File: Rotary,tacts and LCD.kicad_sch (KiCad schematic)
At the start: 53 parts, among them Q1 MMBT3904, SW1 EC11E18244AU, U14 RT9193-18GB, U4 AP3032KTR-G1, U7 IS31FL3733B-QFLS4-TR

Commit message: Updated the net labels for 3v3 and sys rail
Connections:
- net +3V3 is gone; now on net ESP_3V3: C21.1, C22.1, C23.1, C24.1, C25.1, C26.1, C27.1, R10.1, R9.1, U7.20 (PVCC_1), U7.29 (PVCC_2), U7.37 (AVCC), U7.38 (DVCC), U7.39 (VIO)
- net Core_5V renamed SYS

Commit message: Did the layout plan
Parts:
- removed L1: 10uH 3×3×1.5 0.72A, symbol Device:L
- added L1: SWPA3015S100MT, SWPA3015S100MT:IND-SMD_L3.0-W3.0_SWPA3010S, symbol SWPA3015S100MT:SWPA3015S100MT
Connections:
- net SYS: now also L1.1
- net at D31.2, U4.1 (SW): now also L1.2
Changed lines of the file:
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@@
 	(wire
 		(pts
+			(xy 87.63 204.47) (xy 101.6 204.47)
+		)
+		(stroke
+			(width 0)
+			(type default)
+		)
+	)
+	(wire
+		(pts
 			(xy 403.86 102.87) (xy 422.91 102.87)
 		)
@@
 	(wire
 		(pts
+			(xy 64.77 204.47) (xy 77.47 204.47)
+		)
+		(stroke
+			(width 0)
+			(type default)
+		)
+	)
+	(wire
+		(pts
 			(xy 346.71 182.88) (xy 346.71 186.69)
 		)
@@
 	(wire
 		(pts
-			(xy 78.74 204.47) (xy 64.77 204.47)
-		)
-		(stroke
-			(width 0)
-			(type default)
-		)
-	)
-	(wire
-		(pts
 			(xy 208.28 86.36) (xy 212.09 86.36)
 		)
@@
 	(wire
 		(pts
-			(xy 86.36 204.47) (xy 101.6 204.47)
-		)
-		(stroke
-			(width 0)
-			(type default)
-		)
-	)
-	(wire
-		(pts
 			(xy 374.65 82.55) (xy 367.03 82.55)
 		)
@@
 	)
 	(symbol
-		(lib_id "Device:L")
-		(at 82.55 204.47 90)
-		(unit 1)
-		(body_style 1)
-		(exclude_from_sim no)
-		(in_bom yes)
-		(on_board yes)
-		(in_pos_files yes)
-		(dnp no)
-		(fields_autoplaced yes)
-		(property "Reference" "L1"
-			(at 82.55 199.39 90)
-			(show_name no)
-			(do_not_autoplace no)
-			(effects
-				(font
-					(size 1.27 1.27)
-				)
-			)
-		)
-		(property "Value" "10uH 3×3×1.5 0.72A"
-			(at 82.55 201.93 90)
-			(show_name no)
-			(do_not_autoplace no)
-			(effects
-				(font
-					(size 1.27 1.27)
-				)
-			)
-		)
-		(property "Footprint" ""
-			(at 82.55 204.47 0)
-			(hide yes)
-			(show_name no)
-			(do_not_autoplace no)
-			(effects
-				(font
-					(size 1.27 1.27)
-				)
-			)
-		)
-		(property "Datasheet" ""
-			(at 82.55 204.47 0)
-			(hide yes)
-			(show_name no)
-			(do_not_autoplace no)
-			(effects
-				(font
-					(size 1.27 1.27)
-				)
-			)
-		)
-		(property "Description" "Inductor"
-			(at 82.55 204.47 0)
-			(hide yes)
-			(show_name no)
-			(do_not_autoplace no)
-			(effects
-				(font
-					(size 1.27 1.27)
-				)
-			)
-		)
-		(property "Availability" ""
-			(at 82.55 204.47 90)
-			(hide yes)
-			(show_name no)
-			(do_not_autoplace no)
-			(effects
-				(font
-					(size 1.27 1.27)
-				)
-			)
-		)
-		(property "Check_prices" ""
-			(at 82.55 204.47 90)
-			(hide yes)
-			(show_name no)
-			(do_not_autoplace no)
-			(effects
-				(font
-					(size 1.27 1.27)
-				)
-			)
-		)
-		(property "Height" ""
-			(at 82.55 204.47 90)
-			(hide yes)
-			(show_name no)
-			(do_not_autoplace no)
-			(effects
-				(font
-					(size 1.27 1.27)
-				)
-			)
-		)
-		(property "MF" ""
-			(at 82.55 204.47 90)
-			(hide yes)
-			(show_name no)
-			(do_not_autoplace no)
-			(effects
-				(font
-					(size 1.27 1.27)
-				)
-			)
-		)
-		(property "MP" ""
-			(at 82.55 204.47 90)
-			(hide yes)
-			(show_name no)
-			(do_not_autoplace no)
-			(effects
-				(font
-					(size 1.27 1.27)
-				)
-			)
-		)
-		(property "Manufacturer_Name" ""
-			(at 82.55 204.47 90)
-			(hide yes)
-			(show_name no)
-			(do_not_autoplace no)
-			(effects
-				(font
-					(size 1.27 1.27)
-				)
-			)
-		)
-		(property "Manufacturer_Part_Number" ""
-			(at 82.55 204.47 90)
-			(hide yes)
-			(show_name no)
-			(do_not_autoplace no)
-			(effects
-				(font
-					(size 1.27 1.27)
-				)
-			)
-		)
-		(property "Mouser Part Number" ""
-			(at 82.55 204.47 90)
-			(hide yes)
-			(show_name no)
-			(do_not_autoplace no)
-			(effects
-				(font
-					(size 1.27 1.27)
-				)
-			)
-		)
-		(property "Mouser Price/Stock" ""
-			(at 82.55 204.47 90)
-			(hide yes)
-			(show_name no)
-			(do_not_autoplace no)
-			(effects
-				(font
-					(size 1.27 1.27)
-				)
-			)
-		)
-		(property "Package" ""
-			(at 82.55 204.47 90)
-			(hide yes)
-			(show_name no)
-			(do_not_autoplace no)
-			(effects
-				(font
-					(size 1.27 1.27)
-				)
-			)
-		)
-		(property "STANDARD" ""
-			(at 82.55 204.47 90)
-			(hide yes)
-			(show_name no)
-			(do_not_autoplace no)
-			(effects
-				(font
-					(size 1.27 1.27)
-				)
-			)
-		)
-		(property "SnapEDA_Link" ""
-			(at 82.55 204.47 90)
-			(hide yes)
-			(show_name no)
-			(do_not_autoplace no)
-			(effects
-				(font
-					(size 1.27 1.27)
-				)
-			)
-		)
-		(pin "2"
-		)
-		(pin "1"
-		)
-		(instances
-			(project "Galatea Keyboard PCB"
-				(path "/04167948-25c2-4ca8-b9d8-855756010414/f6cda99c-23a6-4328-98ed-312da4a40ab9"
-					(reference "L1")
-					(unit 1)
-				)
-			)
-		)
-	)
-	(symbol
 		(lib_id "Device:C_Small")
 		(at 43.18 349.25 0)
@@
 					(unit 1)
 				)
+			)
+		)
+	)
+	(symbol
+		(lib_id "SWPA3015S100MT:SWPA3015S100MT")
+		(at 82.55 204.47 0)
+		(unit 1)
+		(body_style 1)
+		(exclude_from_sim no)
+		(in_bom yes)
+		(on_board yes)
+		(in_pos_files yes)
+		(dnp no)
+		(fields_autoplaced yes)
+		(property "Reference" "L1"
+			(at 82.52 198.12 0)
+			(show_name no)
+			(do_not_autoplace no)
+			(effects
+				(font
+					(size 1.27 1.27)
+				)
+			)
+		)
+		(property "Value" "SWPA3015S100MT"
+			(at 82.52 200.66 0)
+			(show_name no)
+			(do_not_autoplace no)
+			(effects
+				(font
+					(size 1.27 1.27)
+				)
+			)
+		)
+		(property "Footprint" "SWPA3015S100MT:IND-SMD_L3.0-W3.0_SWPA3010S"
+			(at 82.55 212.09 0)
+			(hide yes)
+			(show_name no)
+			(do_not_autoplace no)
+			(effects
+				(font
+					(size 1.27 1.27)
+				)
+			)
+		)
+		(property "Datasheet" "https://lcsc.com/product-detail/Power-Inductors_10uH-20_C45403.html"
+			(at 82.55 214.63 0)
+			(hide yes)
+			(show_name no)
+			(do_not_autoplace no)
+			(effects
+				(font
+					(size 1.27 1.27)
+				)
+			)
+		)
+		(property "Description" "10uH ±20%"
+			(at 82.55 204.47 0)
+			(hide yes)
+			(show_name no)
+			(do_not_autoplace no)
+			(effects
+				(font
+					(size 1.27 1.27)
+				)
+			)
+		)
+		(property "Manufacturer" "Sunlord(顺络)"
+			(at 82.55 217.17 0)
+			(hide yes)
+			(show_name no)
+			(do_not_autoplace no)
+			(effects
+				(font
+					(size 1.27 1.27)
+				)
+			)
+		)
+		(property "MPN" "SWPA3015S100MT"
+			(at 82.55 219.71 0)
+			(hide yes)
+			(show_name no)
+			(do_not_autoplace no)
+			(effects
+				(font
+					(size 1.27 1.27)
+				)
+			)
+		)
+		(property "LCSC Part" "C45403"
+			(at 82.55 222.25 0)
+			(hide yes)
+			(show_name no)
+			(do_not_autoplace no)
+			(effects
+				(font
+					(size 1.27 1.27)
+				)
+			)
+		)
+		(pin "1"
+		)
+		(pin "2"
+		)
+		(instances
+			(project "Galatea Keyboard PCB"
+				(path "/04167948-25c2-4ca8-b9d8-855756010414/f6cda99c-23a6-4328-98ed-312da4a40ab9"
+					(reference "L1")
+					(unit 1)
+				)

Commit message: Progress on the PCB routing
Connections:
- net DSI_CLKN renamed DSI_CLK_N
- net DSI_CLKP renamed DSI_CLK_P
- net DSI_DATAN0 renamed DSI_DATA0_N
- net DSI_DATAN1 renamed DSI_DATA1_N
- net DSI_DATAP0 renamed DSI_DATA0_P
- net DSI_DATAP1 renamed DSI_DATA1_P
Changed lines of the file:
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@@
 		)
 	)
-	(hierarchical_label "DSI_CLKP"
+	(hierarchical_label "DSI_CLK_P"
 		(shape input)
 		(at 208.28 99.06 180)
@@
 		)
 	)
-	(hierarchical_label "DSI_DATAP1"
+	(hierarchical_label "DSI_DATA1_P"
 		(shape input)
 		(at 208.28 91.44 180)
@@
 		)
 	)
-	(hierarchical_label "DSI_CLKN"
+	(hierarchical_label "DSI_CLK_N"
 		(shape input)
 		(at 208.28 96.52 180)
@@
 		)
 	)
-	(hierarchical_label "DSI_DATAN0"
+	(hierarchical_label "DSI_DATA0_N"
 		(shape input)
 		(at 208.28 81.28 180)
@@
 		)
 	)
-	(hierarchical_label "DSI_DATAN1"
+	(hierarchical_label "DSI_DATA1_N"
 		(shape input)
 		(at 208.28 88.9 180)
@@
 		)
 	)
-	(hierarchical_label "DSI_DATAP0"
+	(hierarchical_label "DSI_DATA0_P"
 		(shape input)
 		(at 208.28 83.82 180)

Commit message: Finalizing the routing
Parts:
- removed DT7: WHITE, LED_SMD:LED_0603_1608Metric, symbol Device:LED
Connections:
- net SW_2: no longer names the net of U7.3 (SW2)
- no-connect marks 32 -> 33

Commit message: Done with the routing. Yet to correct the issue raised and review the whole design
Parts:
- S1: now not fitted; now left out of the parts list

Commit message: Done with the correction, PCB is complete
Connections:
- net I2C1_SCL renamed I2C0_SCL
- net I2C1_SDA renamed I2C0_SDA
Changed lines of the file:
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@@
+		)
+	)
+	(hierarchical_label "I2C0_SCL"
+		(shape output)
+		(at 293.37 74.93 180)
+		(effects
+			(font
+				(size 1.27 1.27)
+			)
+			(justify right)
+		)
+	)
+	(hierarchical_label "I2C0_SDA"
+		(shape output)
+		(at 293.37 72.39 180)
+		(effects
+			(font
+				(size 1.27 1.27)
+			)
+			(justify right)
 		)
 	)
@@
 		)
 	)
-	(hierarchical_label "I2C1_SDA"
-		(shape output)
-		(at 293.37 72.39 180)
-		(effects
-			(font
-				(size 1.27 1.27)
-			)
-			(justify right)
-		)
-	)
 	(hierarchical_label "DSI_DATA0_P"
 		(shape input)
@@
 		(effects
 			(font
-				(size 1.27 1.27)
-			)
-			(justify right)
-		)
-	)
-	(hierarchical_label "I2C1_SCL"
-		(shape output)
-		(at 293.37 74.93 180)
-		(effects
-			(font

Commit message: Corrected the issues raised
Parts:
- added R55: 10kΩ, PCM_JLCPCB:R_0603, symbol PCM_JLCPCB-Resistors:0603,10kΩ
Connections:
- net GND: now also R55.1
- net RESET renamed LCD_RESET
- net LCD_RESET: now also R55.2
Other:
- note added: "VLED+"
- note added: "VLED-"

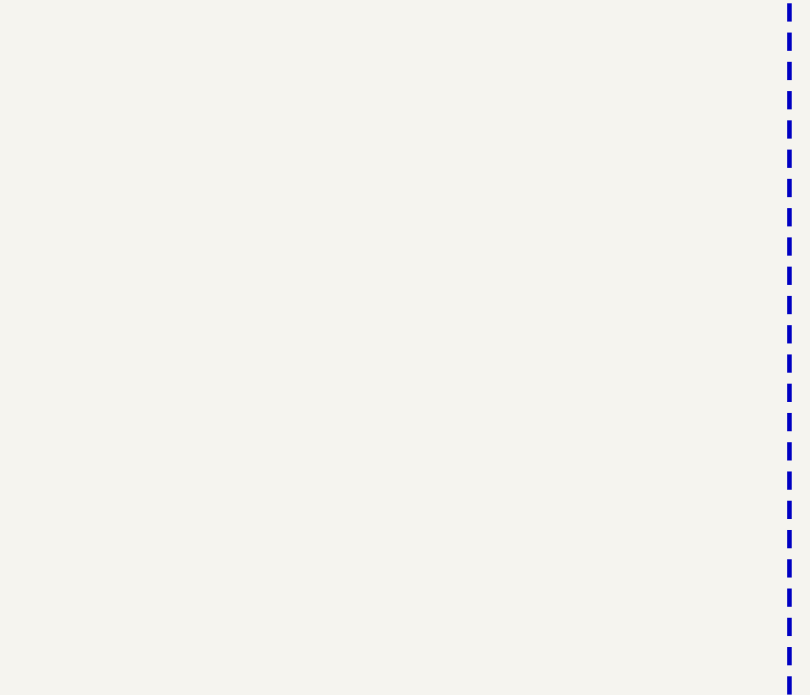
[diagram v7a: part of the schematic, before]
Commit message: Added GT911 connector and fix the USB_C issue
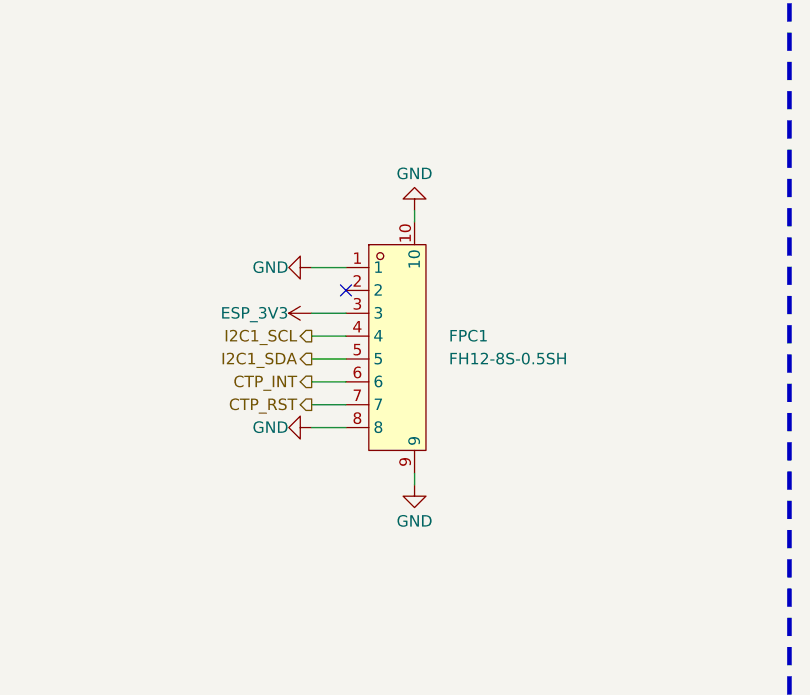
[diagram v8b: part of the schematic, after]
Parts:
- added FPC1: FH12-8S-0.5SH, FH12-8S-0.5SH(55):FPC-SMD_8P-P0.50_FH12S-8S-0.5SH-55, symbol FH12-8S-0.5SH(55):FH12-8S-0.5SH
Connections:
- net ESP_3V3: now also FPC1.3
- net GND: now also FPC1.1, FPC1.10, FPC1.8, FPC1.9
- new net CTP_INT: FPC1.6
- new net CTP_RST: FPC1.7
- new net I2C1_SCL: FPC1.4
- new net I2C1_SDA: FPC1.5
- no-connect marks 33 -> 34
